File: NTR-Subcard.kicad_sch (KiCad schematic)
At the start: 6 parts, among them CN1 Conn_01x40_Pin, U1 M95256-WMN6P, U2 M45PE20-VMN6P

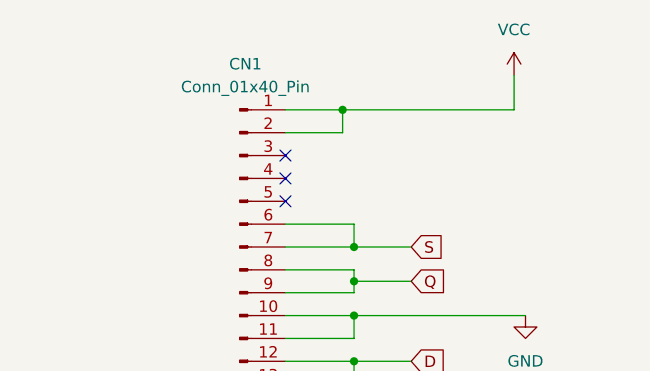
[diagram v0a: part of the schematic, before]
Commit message: Rename CN1, add pdf file
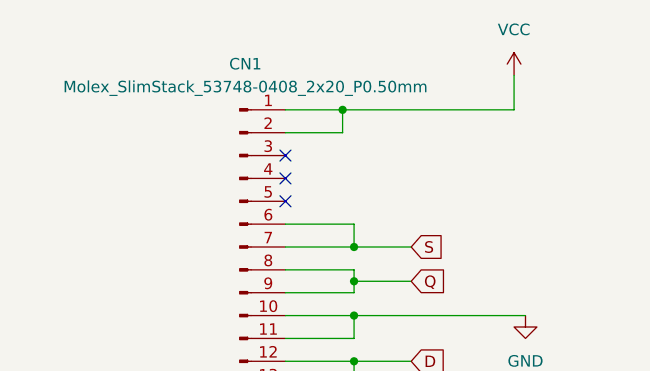
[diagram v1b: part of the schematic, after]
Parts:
- CN1: value Conn_01x40_Pin -> Molex_SlimStack_53748-0408_2x20_P0.50mm
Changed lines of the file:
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@@
 			)
 		)
-		(property "Value" "Conn_01x40_Pin"
+		(property "Value" "Molex_SlimStack_53748-0408_2x20_P0.50mm"
 			(at 51.435 35.56 0)
 			(effects

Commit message: Updates after first production batch
Signed-off-by: rosaage <tagemellemstrand@hotmail.com>
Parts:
- R1: value R -> 10k
- U1: value M95256-WMN6P -> M95512-WMN6P; now left out of the parts list
- U2: footprint Package_SO:SOIC-8_3.9x4.9mm_P1.27mm -> tage:SOIC-8_3.9x3.9-7.62mm_P1.27mm; now left out of the parts list
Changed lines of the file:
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@@
+			)
+		)
+		(property "LCSC Part Number" ""
+			(at 143.51 99.06 0)
+			(effects
+				(font
+					(size 1.27 1.27)
+				)
+				(hide yes)
 			)
 		)
@@
 		(unit 1)
 		(exclude_from_sim no)
-		(in_bom yes)
+		(in_bom no)
 		(on_board yes)
 		(dnp no)
@@
 			)
 		)
-		(property "Footprint" "Package_SO:SOIC-8_3.9x4.9mm_P1.27mm"
+		(property "Footprint" "tage:SOIC-8_3.9x3.9-7.62mm_P1.27mm"
 			(at 180.34 43.18 0)
 			(effects
@@
 			)
 		)
+		(property "LCSC Part Number" ""
+			(at 179.07 62.23 0)
+			(effects
+				(font
+					(size 1.27 1.27)
+				)
+				(hide yes)
+			)
+		)
 		(pin "1"
 		)
@@
 			)
 		)
-		(property "Value" "R"
+		(property "Value" "10k"
 			(at 156.21 59.6899 0)
 			(effects
@@
 			)
 		)
+		(property "LCSC Part Number" ""
+			(at 153.67 58.42 0)
+			(effects
+				(font
+					(size 1.27 1.27)
+				)
+				(hide yes)
+			)
+		)
 		(pin "1"
 		)
@@
 			)
 		)
+		(property "LCSC Part Number" ""
+			(at 50.8 86.36 0)
+			(effects
+				(font
+					(size 1.27 1.27)
+				)
+				(hide yes)
+			)
+		)
 		(pin "20"
 		)
@@
 		(unit 1)
 		(exclude_from_sim no)
-		(in_bom yes)
+		(in_bom no)
 		(on_board yes)
 		(dnp no)
@@
 			)
 		)
-		(property "Value" "M95256-WMN6P"
+		(property "Value" "M95512-WMN6P"
 			(at 158.4041 124.46 0)
 			(effects
@@
 			)
 		)
+		(property "LCSC Part Number" ""
+			(at 156.21 114.3 0)
+			(effects
+				(font
+					(size 1.27 1.27)
+				)
+				(hide yes)
+			)
+		)
 		(pin "1"
 		)
@@
 			(at 186.69 44.45 0)
 			(effects
+				(font
+					(size 1.27 1.27)
+				)
+				(hide yes)
+			)
+		)
+		(property "LCSC Part Number" ""
+			(at 186.69 44.45 0)
+			(effects
